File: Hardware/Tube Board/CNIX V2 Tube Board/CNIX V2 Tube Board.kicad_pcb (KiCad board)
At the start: 2 copper layers, 185 x 51 mm, 50 parts, among them J1 VDD, J2 GND, J3 Tube Conn, J4 LED, J5 HT, U1 SN75468, U10 IN-4_0, U11 IN-4_1, U12 IN-4_2, U13 IN-4_3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

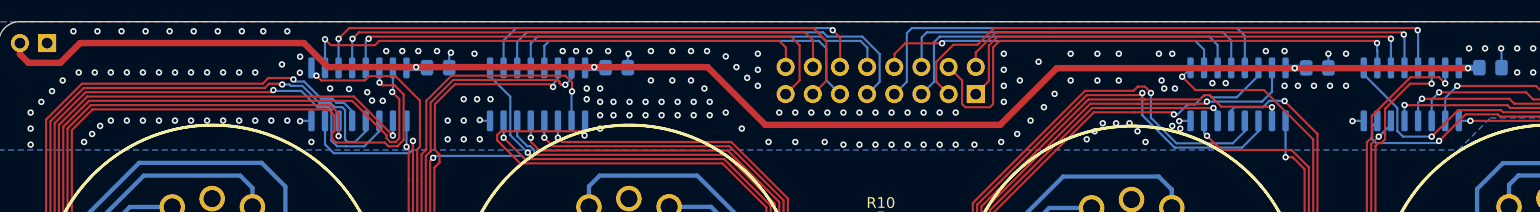
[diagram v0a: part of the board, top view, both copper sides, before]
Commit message: added silkscreen and updated gerbers
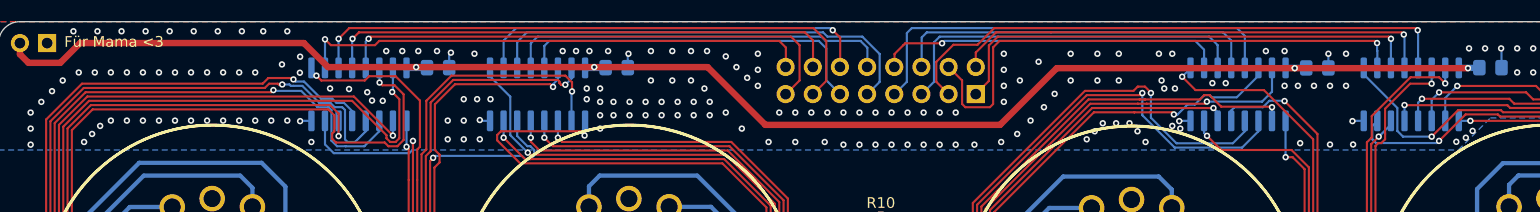
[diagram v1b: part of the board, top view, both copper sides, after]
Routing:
- net GND: vias 218 -> 224
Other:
- board text added: "Für Mama <3"
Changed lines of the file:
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@@
 		(layer "User.1")
+	)
+	(gr_text "Für Mama <3"
+		(at 72.136 77.47 0)
+		(layer "F.SilkS")
+		(effects
+			(font
+				(size 1 1)
+				(thickness 0.15)
+			)
+			(justify left bottom)
+		)
 	)
 	(dimension
@@
 	)
 	(via
+		(at 203.2 85.852)
+		(size 0.6)
+		(drill 0.3)
+		(layers "F.Cu" "B.Cu")
+		(free yes)
+		(net 3)
+	)
+	(via
 		(at 137 78)
 		(size 0.6)
@@
 	)
 	(via
+		(at 192.659 86.487)
+		(size 0.6)
+		(drill 0.3)
+		(layers "F.Cu" "B.Cu")
+		(free yes)
+		(net 3)
+	)
+	(via
 		(at 128 82.5)
 		(size 0.6)
@@
 	)
 	(via
+		(at 187.706 86.36)
+		(size 0.6)
+		(drill 0.3)
+		(layers "F.Cu" "B.Cu")
+		(free yes)
+		(net 3)
+	)
+	(via
 		(at 135 79.25)
 		(size 0.6)
@@
 	)
 	(via
+		(at 203.835 85.217)
+		(size 0.6)
+		(drill 0.3)
+		(layers "F.Cu" "B.Cu")
+		(free yes)
+		(net 3)
+	)
+	(via
 		(at 98.775 81.3)
 		(size 0.6)
@@
 	)
 	(via
+		(at 202.311 86.233)
+		(size 0.6)
+		(drill 0.3)
+		(layers "F.Cu" "B.Cu")
+		(free yes)
+		(net 3)
+	)
+	(via
 		(at 149.5 86.5)
 		(size 0.6)
@@
 		(size 0.6)
 		(drill 0.3)
+		(layers "F.Cu" "B.Cu")
+		(free yes)
+		(net 3)
+	)
+	(via
+		(at 190.5 86.487)
+		(size 0.6)
+		(drill 0.3)
